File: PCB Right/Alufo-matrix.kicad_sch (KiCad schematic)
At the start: 63 parts, among them K11 PG1350, K12 PG1350, K13 PG1350, K14 PG1350, K15 PG1350, K16 PG1350, K21 PG1350, K22 PG1350, K23 PG1350, K24 PG1350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

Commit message: Update project library name in schematic
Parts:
- D11, D12, D13, D14, D15, D16, D21, D22, D23, D24, D25, D26, D32, D33, D34, D35: footprint Project Library:D_SOD-123_Mod -> Project_Library:D_SOD-123_Mod
- D41, D42, D43, D44, D45, D46: footprint Project Library:D_SOD-123 -> Project_Library:D_SOD-123
- K11, K12, K13, K14, K15, K16, K21, K22, K23, K24, K25, K26, K32, K33, K34, K35: footprint Project Library:SW_choc_v1_HS_CPG135001S30_1layer_1u -> Project_Library:SW_choc_v1_HS_CPG135001S30_1layer_1u
- K41: footprint Project Library:SW_choc_v1_HS_CPG135001S30_1layer_1.5u -> Project_Library:SW_choc_v1_HS_CPG135001S30_1layer_1.5u
- K42: footprint Project Library:SW_choc_v1_HS_nav_CPG135001S30_SKQUCAA010_1layer_1u_1 -> Project_Library:SW_choc_v1_HS_nav_CPG135001S30_SKQUCAA010_1layer_1u_1; symbol Project Library:SW_SP5T -> Project_Library:SW_SP5T
- PK11, PK12, PK13, PK14, PK15, PK16, PK21, PK22, PK23, PK24, PK25, PK26, PK32, PK33, PK34, PK35, PK42: footprint Project Library:SW_choc_v1_Plate_CPG135001S30_1u -> Project_Library:SW_choc_v1_Plate_CPG135001S30_1u
- PK41: footprint Project Library:SW_choc_v1_Plate_CPG135001S30_1.5u -> Project_Library:SW_choc_v1_Plate_CPG135001S30_1.5u

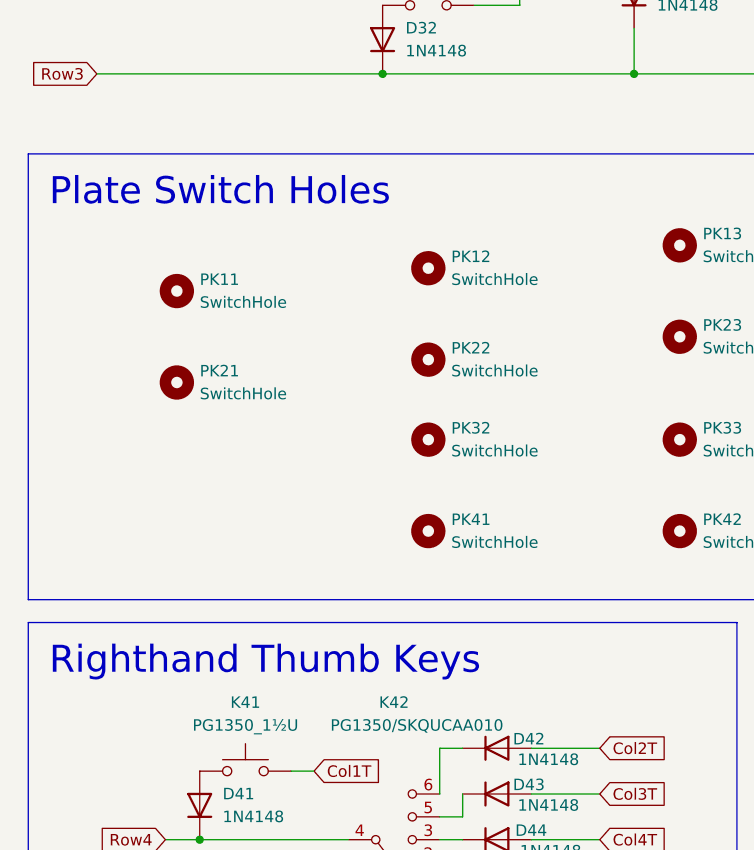
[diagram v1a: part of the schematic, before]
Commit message: Update to KiCad v9
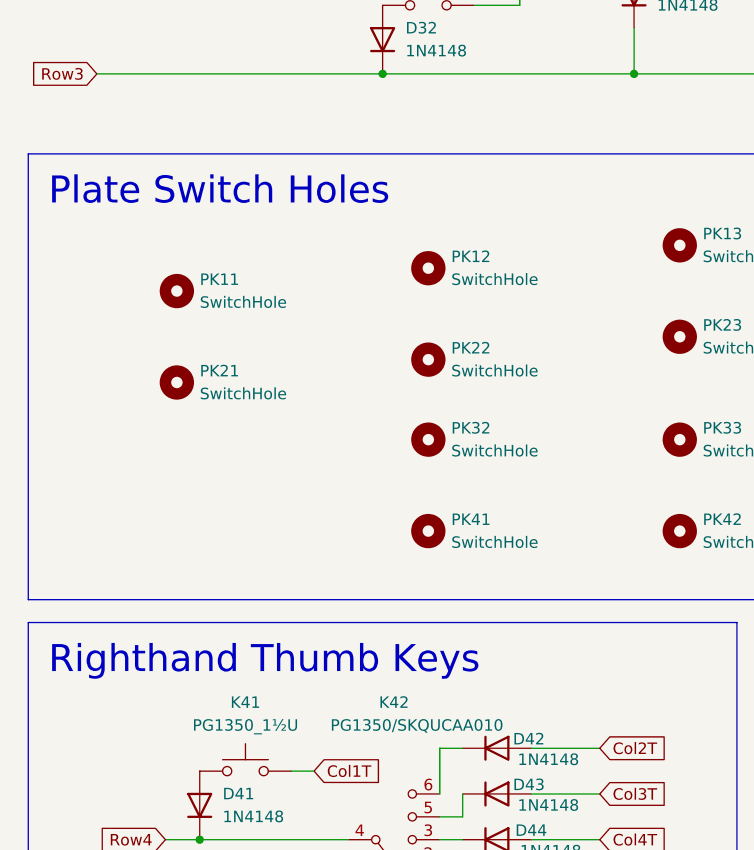
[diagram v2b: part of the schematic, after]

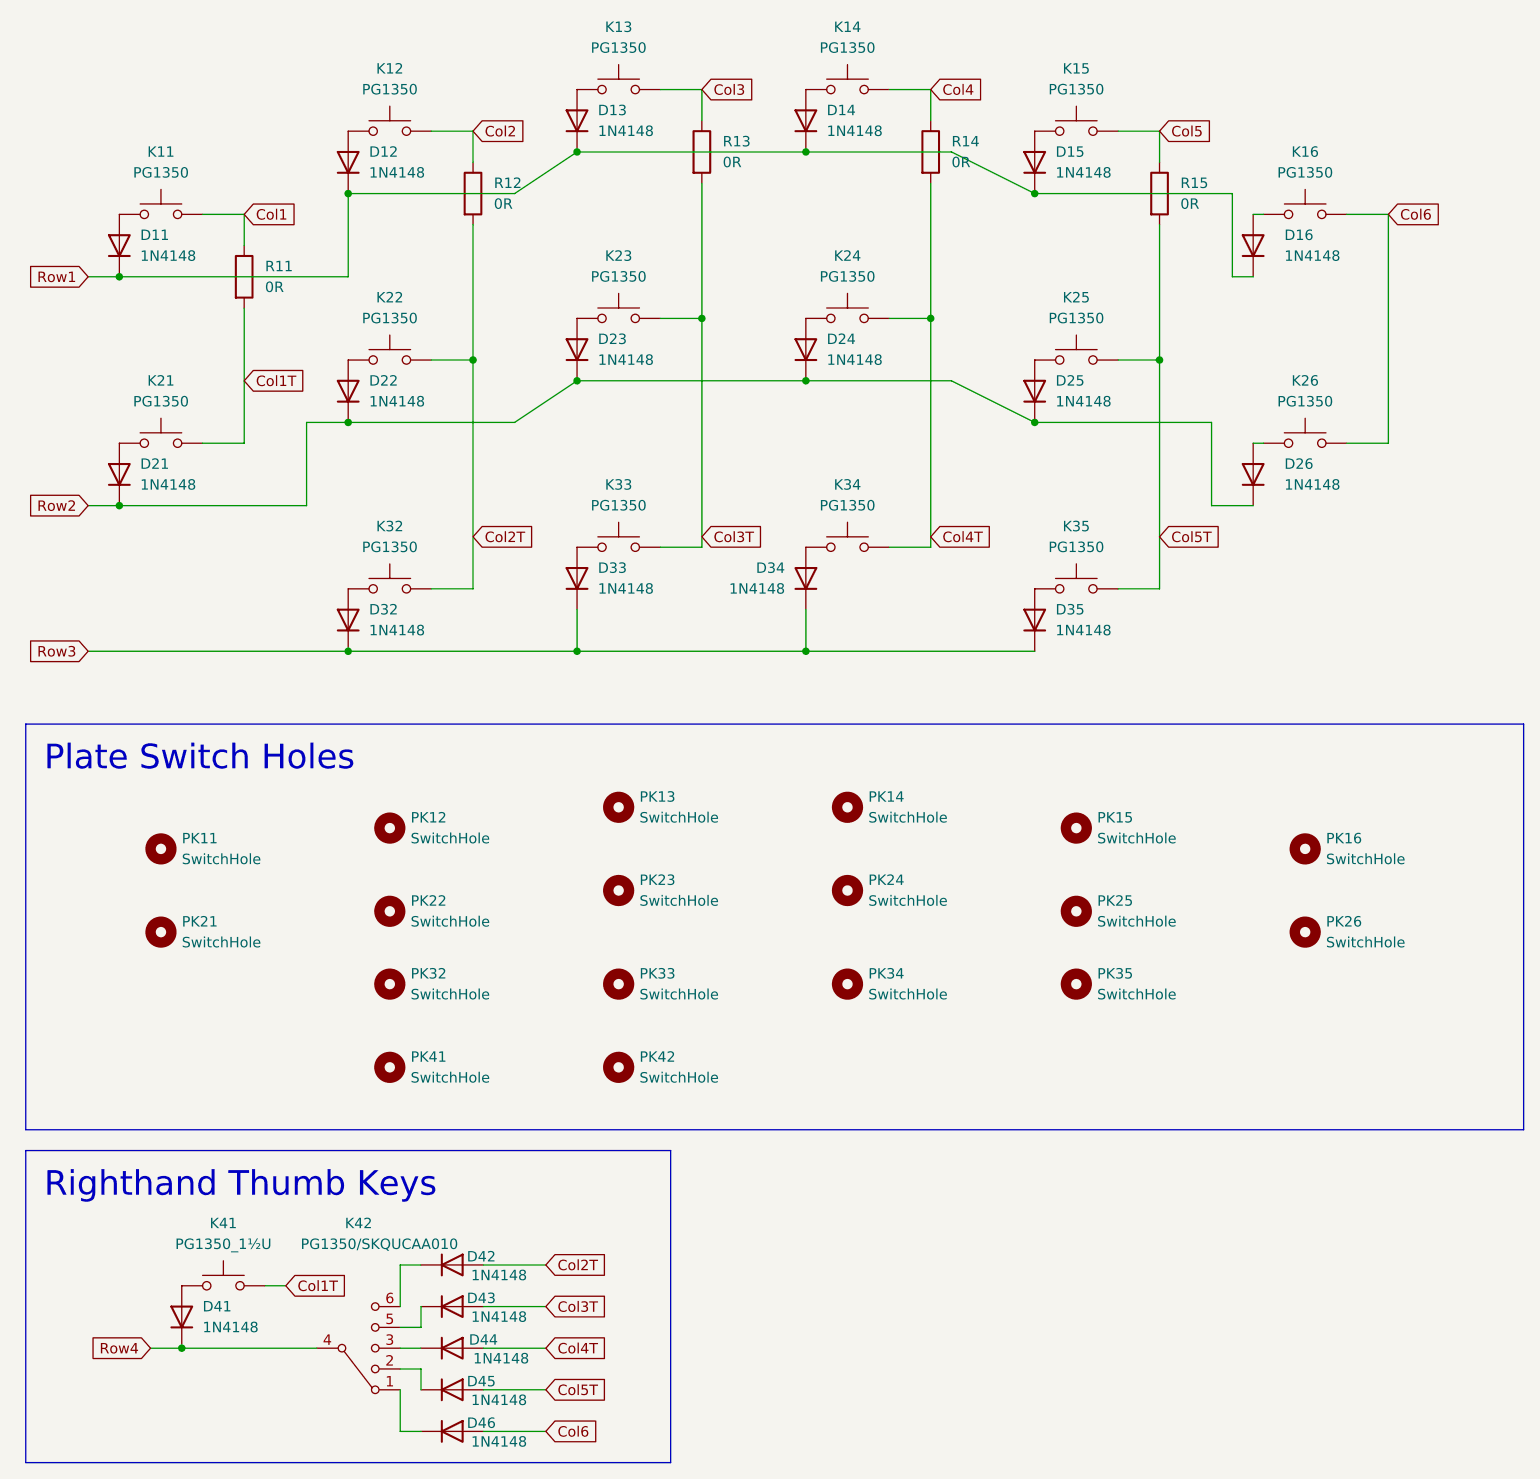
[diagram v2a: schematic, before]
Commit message: Update right side
Also add outline for middle layer to new USB port footprint (although it won’t be right.
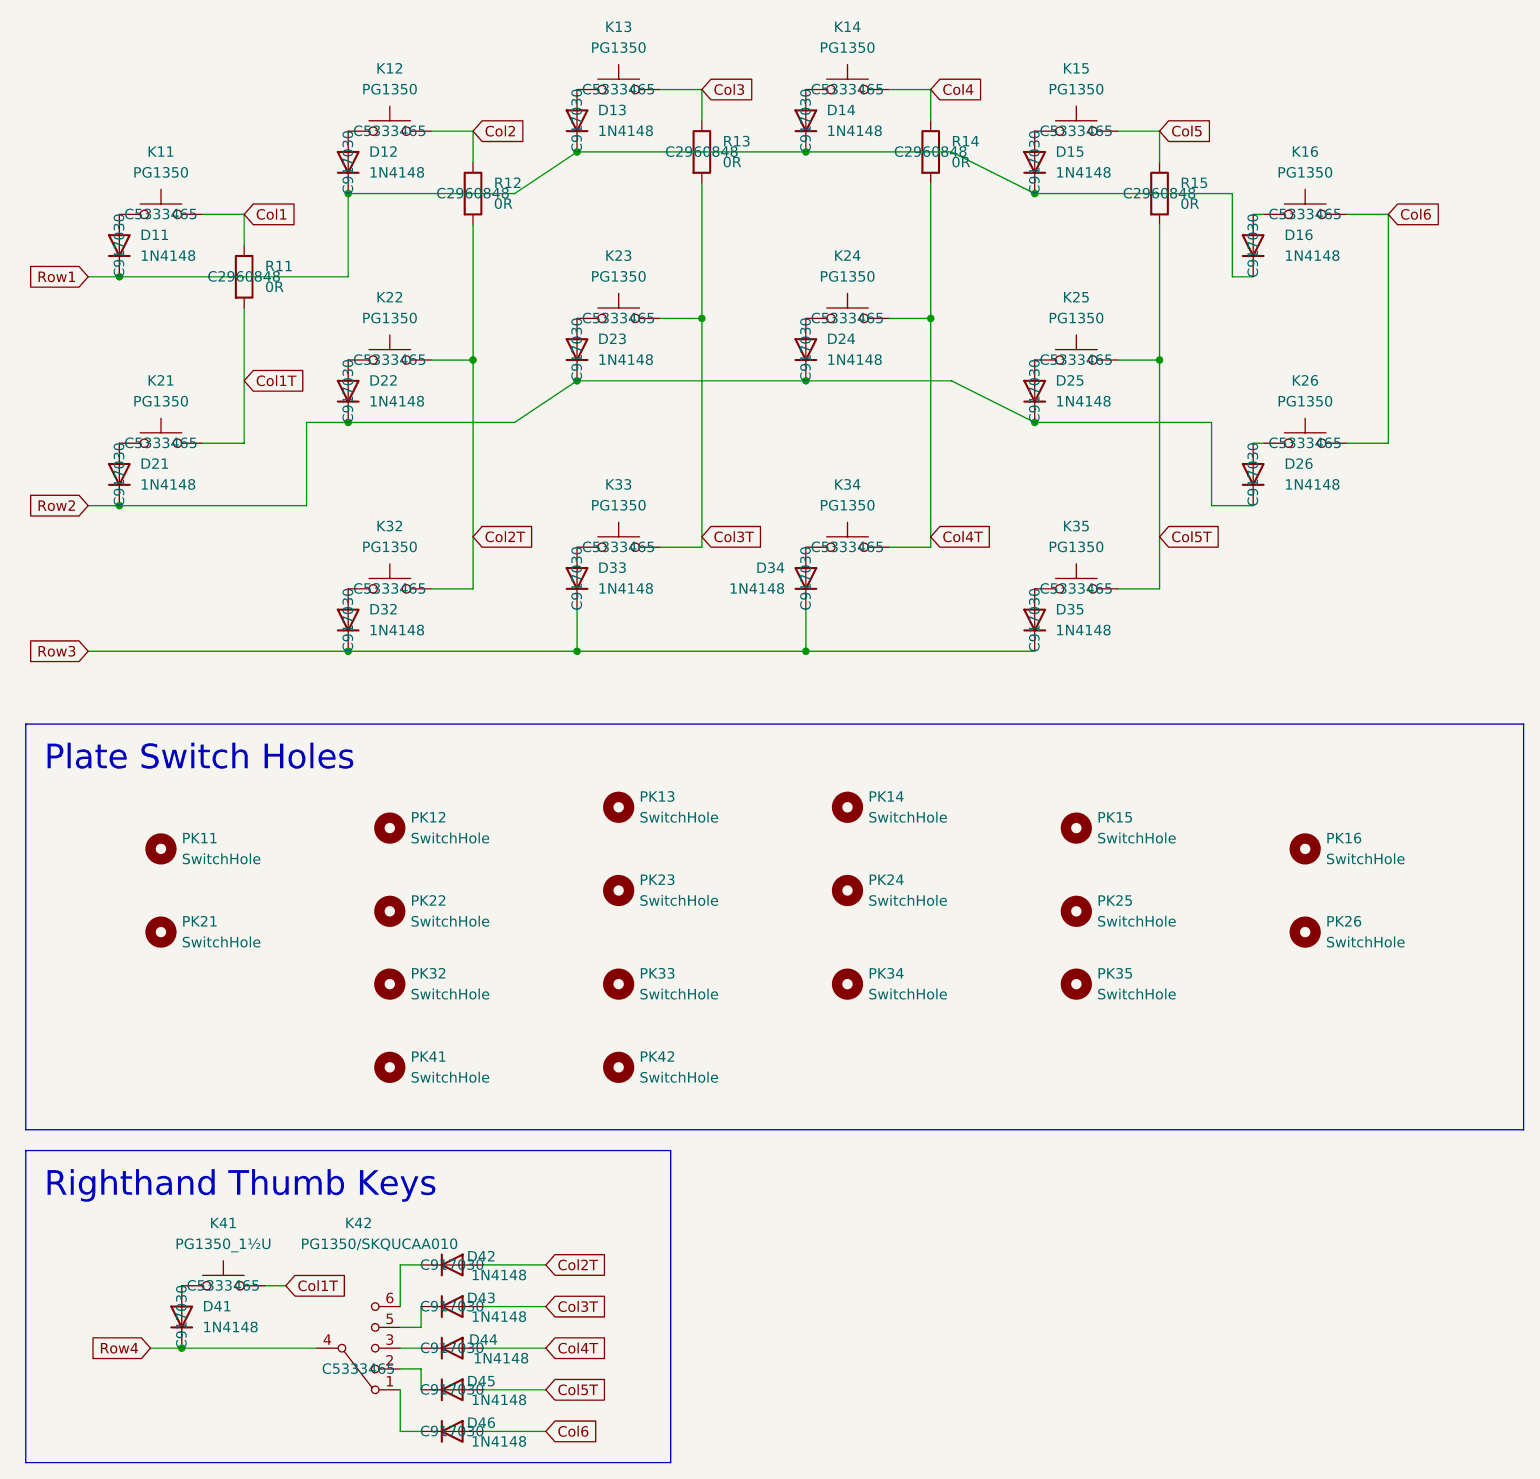
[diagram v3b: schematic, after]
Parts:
- D11, D12, D13, D14, D15, D16, D21, D22, D23, D24, D25, D26, D32, D33, D34, D35, D41, D42, D43, D44, D45, D46: LCSC (none) -> C917030
- K11, K12, K13, K14, K15, K16, K21, K22, K23, K24, K25, K26, K32, K33, K34, K35, K41, K42: LCSC (none) -> C5333465
- R11, R12, R13, R14, R15: LCSC (none) -> C2960848

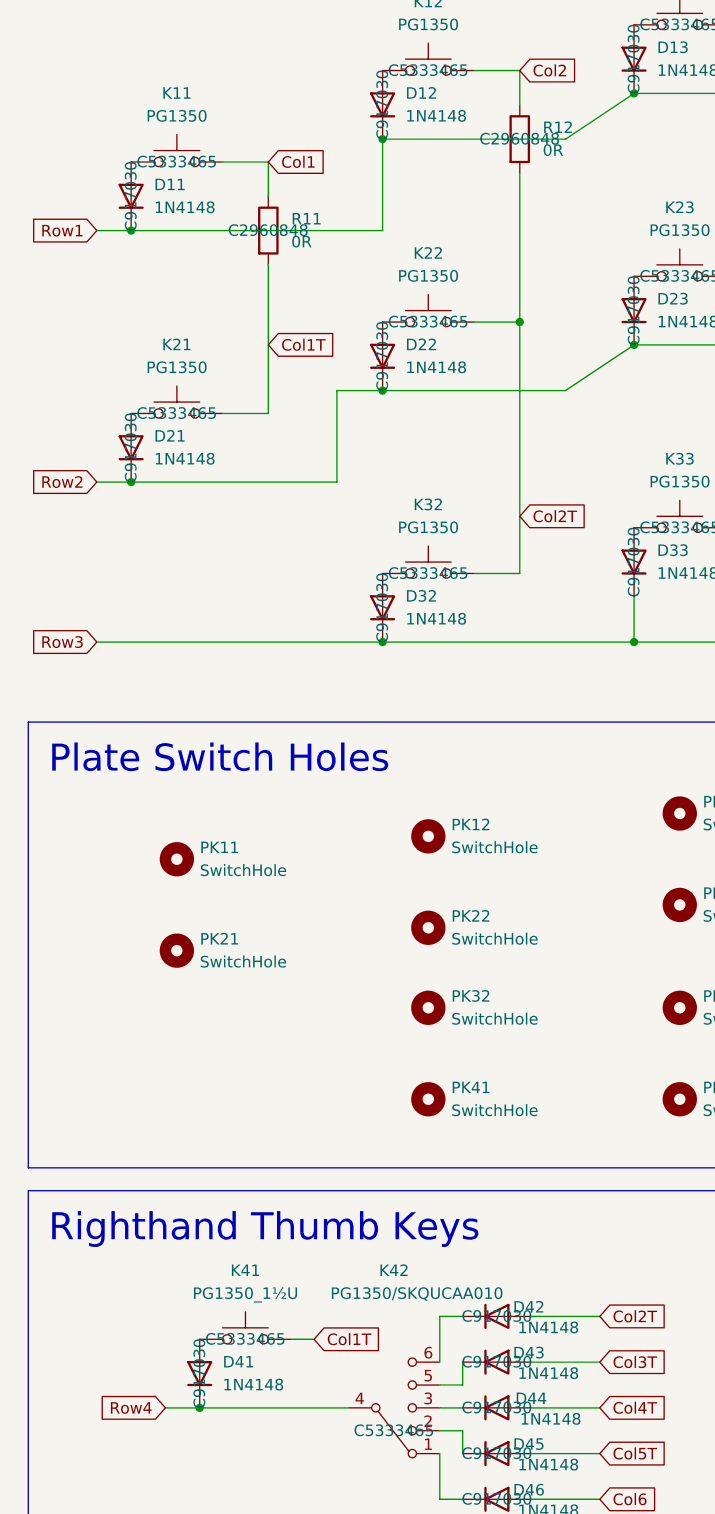
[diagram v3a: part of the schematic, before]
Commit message: Remove righthand R11
Col1 now routed under MCU between K11 and K21 instead of through jumper.
Row1 and Col1 pins on MCU swapped.
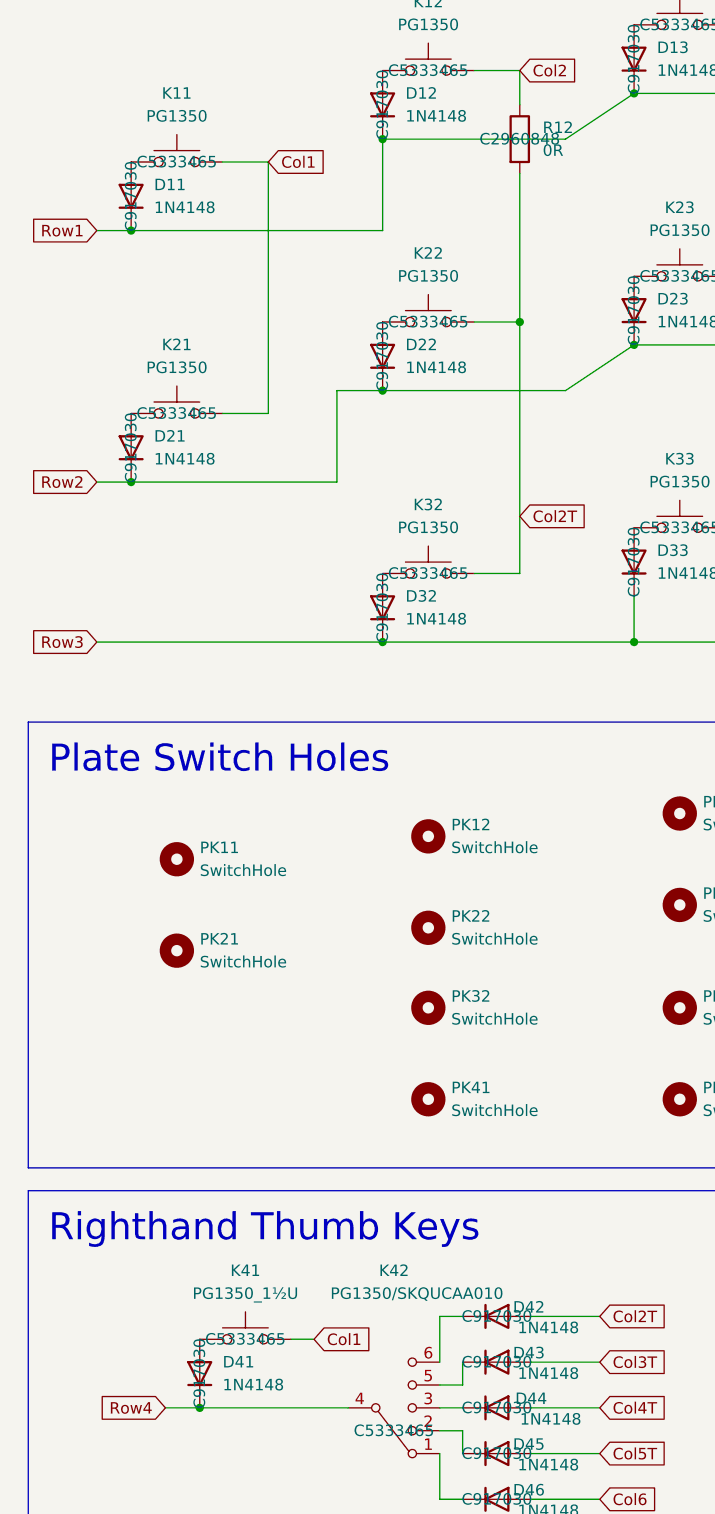
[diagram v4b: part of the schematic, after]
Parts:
- removed R11: 0R, Resistor_SMD:R_2010_5025Metric, symbol Device:R
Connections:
- net Col1T is gone; now on net Col1: K21.1, K41.1
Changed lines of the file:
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@@
-	(wire
-		(pts
-			(xy 87.63 54.61) (xy 87.63 71.12)
-		)
-		(stroke
-			(width 0)
-			(type default)
-		)
-	)
 	(wire
 		(pts
@@
 	(wire
 		(pts
-			(xy 87.63 43.18) (xy 87.63 46.99)
+			(xy 87.63 43.18) (xy 87.63 71.12)
 		)
 		(stroke
@@
 		)
 	)
-	(global_label "Col1T"
+	(global_label "Col1"
 		(shape input)
 		(at 92.71 173.99 0)
@@
 		)
 		(property "Intersheetrefs" "${INTERSHEET_REFS}"
-			(at 100.9565 173.99 0)
+			(at 98.824 173.99 0)
 			(effects
 				(font
@@
 		(property "Intersheetrefs" "${INTERSHEET_REFS}"
 			(at 207.6365 82.55 0)
-			(effects
-				(font
-					(size 1.27 1.27)
-				)
-				(justify left)
-				(hide yes)
-			)
-		)
-	)
-	(global_label "Col1T"
-		(shape input)
-		(at 87.63 63.5 0)
-		(fields_autoplaced yes)
-		(effects
-			(font
-				(size 1.27 1.27)
-			)
-			(justify left)
-		)
-		(property "Intersheetrefs" "${INTERSHEET_REFS}"
-			(at 95.8765 63.5 0)
 			(effects
 				(font
@@
 					(unit 1)
 				)
-			)
-		)
-	)
-	(symbol
-		(lib_id "Device:R")
-		(at 87.63 50.8 0)
-		(unit 1)
-		(exclude_from_sim no)
-		(in_bom yes)
-		(on_board yes)
-		(dnp no)
-		(property "Reference" "R11"
-			(at 90.17 49.5299 0)
-			(effects
-				(font
-					(size 1.27 1.27)
-				)
-				(justify left)
-			)
-		)
-		(property "Value" "0R"
-			(at 90.17 52.0699 0)
-			(effects
-				(font
-					(size 1.27 1.27)
-				)
-				(justify left)
-			)
-		)
-		(property "Footprint" "Resistor_SMD:R_2010_5025Metric"
-			(at 85.852 50.8 90)
-			(effects
-				(font
-					(size 1.27 1.27)
-				)
-				(hide yes)
-			)
-		)
-		(property "Datasheet" "~"
-			(at 87.63 50.8 0)
-			(effects
-				(font
-					(size 1.27 1.27)
-				)
-				(hide yes)
-			)
-		)
-		(property "Description" "Resistor"
-			(at 87.63 50.8 0)
-			(effects
-				(font
-					(size 1.27 1.27)
-				)
-				(hide yes)
-			)
-		)
-		(property "LCSC" "C2960848"
-			(at 87.63 50.8 0)
-			(effects
-				(font
-					(size 1.27 1.27)
-				)
-			)
-		)
-		(pin "1"
-		)
-		(pin "2"
-		)
-		(instances
-			(project "Alufo"
-				(path "/52f043ac-ccff-4c85-bc10-2db9d3c9e3f3/ba0213d9-9934-4194-9bec-bf394cd27126"
-					(reference "R11")
-					(unit 1)
-				)
